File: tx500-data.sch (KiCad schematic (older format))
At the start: 46 parts, among them J1 USB_B_Micro, J2 CAT, J3 REM/DATA, J4 USB_A, U1 TUSB2036, U2 FT232RL, U3 HS-100B, U4 TPS76333, Y1 6MHz

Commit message: Fix floating pins
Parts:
- added R17: 10kΩ, Resistor_SMD:R_1210_3225Metric, symbol Device:R
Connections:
- net labels added: PWREN, SLEEP
- wire segments 155 -> 161
- no-connect marks 59 -> 40
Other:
- note added: "See FT232R datasheet\n6.4 USB Bus Powered with Selectable External Logic Supply"
- note added: "See TUSB2036 datasheet\n9.2.2 Detailed Design Procedure"
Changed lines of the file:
@@
-$EndComp
-$Comp
-L Regulator_Linear:TPS76333 U?
-U 1 1 60701E6D
-P 2250 1200
-AR Path="/6057976E/60701E6D" Ref="U?"  Part="1"
-AR Path="/60701E6D" Ref="U4"  Part="1"
-F 0 "U4" H 2250 1542 50  0000 C CNN
-F 1 "TPS76333" H 2250 1451 50  0000 C CNN
-F 2 "Package_TO_SOT_SMD:SOT-23-5" H 2250 1525 50  0001 C CIN
-F 3 "http://www.ti.com/lit/ds/symlink/tps763.pdf" H 2250 1200 50  0001 C CNN
-F 4 "Voltage Regulator" H 2250 1642 50  0001 C CNN "Description"
-F 5 "TI" H 2250 1642 50  0001 C CNN "Manufacturer_Name"
-F 6 "TPS76333" H 2250 1642 50  0001 C CNN "Manufacturer_Part_Number"
-F 7 "0.97" H 2250 1642 50  0001 C CNN "Price"
-F 8 "595-TPS76333DBVTG4" H 2250 1642 50  0001 C CNN "Vendor Part Number"
-F 9 "Mouser" H 2250 1642 50  0001 C CNN "Vendor"
-	1    2250 1200
-	1    0    0    -1
 $EndComp
 $Comp
@@
 	1400 1150 1400 1100
 Wire Wire Line
-	1400 1100 1950 1100
+	1400 1100 1900 1100
 Wire Wire Line
 	800  1100 1000 1100
@@
 Connection ~ 1400 1100
 Connection ~ 1000 1100
-NoConn ~ 1950 1200
 $Comp
 L Device:R R?
@@
 NoConn ~ 9900 2600
 NoConn ~ 9900 2700
-NoConn ~ 9900 2800
 NoConn ~ 9900 2900
 NoConn ~ 8300 2600
@@
 	9400 6400 9200 6400
 $Comp
-L HS-100B:HS-100B U3
-U 1 1 60A2B59C
-P 8700 6200
-AR Path="/60A2B59C" Ref="U3"  Part="1"
-AR Path="/605AB33C/60A2B59C" Ref="U?"  Part="1"
-F 0 "U3" V 10450 4650 50  0000 R CNN
-F 1 "HS-100B" V 10300 4800 50  0000 R CNN
-F 2 "Package_QFP:LQFP-48_7x7mm_P0.5mm" H 10250 6800 50  0001 L CNN
-F 3 "1.6" H 10250 6700 50  0001 L CNN
-F 4 "USB Audio Interface" H 10250 6600 50  0001 L CNN "Description"
-F 5 "1.6" H 10250 6500 50  0001 L CNN "Height"
-F 6 "Cmedia" H 10250 6400 50  0001 L CNN "Manufacturer_Name"
-F 7 "HS-100B" H 10250 6300 50  0001 L CNN "Manufacturer_Part_Number"
-F 8 "0.78" H 8500 6750 50  0001 C CNN "Price"
-F 9 "HS-100B" H 8500 6750 50  0001 C CNN "Vendor Part Number"
-F 10 "Symmetry" H 8500 6750 50  0001 C CNN "Vendor"
-	1    8700 6200
-	0    -1   -1   0
-$EndComp
-$Comp
 L power:GNDREF #PWR?
 U 1 1 60A2B583
@@
 NoConn ~ 9100 6200
 NoConn ~ 9300 6200
-NoConn ~ 9500 6200
 NoConn ~ 9700 6200
-NoConn ~ 10600 5900
-NoConn ~ 10600 5800
-NoConn ~ 10600 5700
-NoConn ~ 10600 5600
-NoConn ~ 10600 5500
-NoConn ~ 10600 5400
-NoConn ~ 10600 5300
-NoConn ~ 10600 5100
-NoConn ~ 10600 5000
-NoConn ~ 10600 4900
-NoConn ~ 10600 4800
 NoConn ~ 9700 4500
 NoConn ~ 9600 4500
 NoConn ~ 9200 4500
-NoConn ~ 7900 5900
 NoConn ~ 7900 5800
-NoConn ~ 7900 5700
-NoConn ~ 7900 5600
 NoConn ~ 7900 5300
 NoConn ~ 7900 5200
 NoConn ~ 7900 5000
-NoConn ~ 7900 4900
-NoConn ~ 7900 4800
 Wire Wire Line
 	7250 5400 7900 5400
@@
 Text Notes 950  5800 0    118  ~ 0
 PCB
-Text Notes 10300 2750 0    50   ~ 0
+Text Notes 10350 1950 0    50   ~ 0
 See TX-500 adapters\nAudio data cable
 Wire Wire Line
@@
 	-1   0    0    -1
 $EndComp
+$Comp
+L Regulator_Linear:TPS76333 U?
+U 1 1 60701E6D
+P 2250 1200
+AR Path="/6057976E/60701E6D" Ref="U?"  Part="1"
+AR Path="/60701E6D" Ref="U4"  Part="1"
+F 0 "U4" H 2250 1542 50  0000 C CNN
+F 1 "TPS76333" H 2250 1451 50  0000 C CNN
+F 2 "Package_TO_SOT_SMD:SOT-23-5" H 2250 1525 50  0001 C CIN
+F 3 "http://www.ti.com/lit/ds/symlink/tps763.pdf" H 2250 1200 50  0001 C CNN
+F 4 "Voltage Regulator" H 2250 1642 50  0001 C CNN "Description"
+F 5 "TI" H 2250 1642 50  0001 C CNN "Manufacturer_Name"
+F 6 "TPS76333" H 2250 1642 50  0001 C CNN "Manufacturer_Part_Number"
+F 7 "0.97" H 2250 1642 50  0001 C CNN "Price"
+F 8 "595-TPS76333DBVTG4" H 2250 1642 50  0001 C CNN "Vendor Part Number"
+F 9 "Mouser" H 2250 1642 50  0001 C CNN "Vendor"
+	1    2250 1200
+	1    0    0    -1
+$EndComp
+Wire Wire Line
+	1950 1200 1900 1200
+Wire Wire Line
+	1900 1200 1900 1100
+Connection ~ 1900 1100
+Wire Wire Line
+	1900 1100 1950 1100
+$Comp
+L HS-100B:HS-100B U3
+U 1 1 60A2B59C
+P 8700 6200
+AR Path="/60A2B59C" Ref="U3"  Part="1"
+AR Path="/605AB33C/60A2B59C" Ref="U?"  Part="1"
+F 0 "U3" V 10450 4650 50  0000 R CNN
+F 1 "HS-100B" V 10300 4800 50  0000 R CNN
+F 2 "Package_QFP:LQFP-48_7x7mm_P0.5mm" H 10250 6800 50  0001 L CNN
+F 3 "https://datasheet.lcsc.com/szlcsc/1906061502_Cmedia-HS-100B_C371351.pdf" H 10250 6700 50  0001 L CNN
+F 4 "USB Audio Interface" H 10250 6600 50  0001 L CNN "Description"
+F 5 "1.6" H 10250 6500 50  0001 L CNN "Height"
+F 6 "Cmedia" H 10250 6400 50  0001 L CNN "Manufacturer_Name"
+F 7 "HS-100B" H 10250 6300 50  0001 L CNN "Manufacturer_Part_Number"
+F 8 "0.78" H 8500 6750 50  0001 C CNN "Price"
+F 9 "HS-100B" H 8500 6750 50  0001 C CNN "Vendor Part Number"
+F 10 "Symmetry" H 8500 6750 50  0001 C CNN "Vendor"
+	1    8700 6200
+	0    -1   -1   0
+$EndComp
+Text Notes 6400 3350 0    50   ~ 0
+See FT232R datasheet\n6.4 USB Bus Powered with Selectable External Logic Supply
+Text Notes 3800 1200 0    50   ~ 0
+See TUSB2036 datasheet\n9.2.2 Detailed Design Procedure
+Text Label 9900 2800 0    50   ~ 0
+PWREN
+Text Label 9900 2900 0    50   ~ 0
+SLEEP
+$Comp
+L Device:R R?
+U 1 1 605D5F33
+P 10200 2600
+AR Path="/605B3ED2/605D5F33" Ref="R?"  Part="1"
+AR Path="/6059C0E9/605D5F33" Ref="R?"  Part="1"
+AR Path="/605D5F33" Ref="R17"  Part="1"
+F 0 "R17" H 10270 2646 50  0000 L CNN
+F 1 "10kΩ" H 10270 2555 50  0000 L CNN
+F 2 "Resistor_SMD:R_1210_3225Metric" V 10130 2600 50  0001 C CNN
+F 3 "https://www.mouser.com/datasheet/2/427/rcae3-1761931.pdf" H 10200 2600 50  0001 C CNN
+F 4 "Vishay" H 10270 2746 50  0001 C CNN "Manufacturer_Name"
+F 5 "RCA121015K0FKEA" H 10270 2746 50  0001 C CNN "Manufacturer_Part_Number"
+F 6 "0.11" H 10270 2746 50  0001 C CNN "Price"
+F 7 "71-RCA121015K0FKEA" H 10270 2746 50  0001 C CNN "Vendor Part Number"
+F 8 "Mouser" H 10270 2746 50  0001 C CNN "Vendor"
+	1    10200 2600
+	1    0    0    -1
+$EndComp
+Wire Wire Line
+	10200 2750 10200 2800
+Wire Wire Line
+	10200 2800 9900 2800
+Wire Wire Line
+	10200 2450 10650 2450
 $EndSCHEMATC

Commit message: Add case ground
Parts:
- added C18: 4.7μF, Capacitor_SMD:C_1210_3225Metric, symbol Device:C
- added C19: 120μF, Capacitor_SMD:C_1210_3225Metric, symbol Device:C
- C11, C16, C17: value 100μF -> 120μF; Manufacturer_Name AVX -> (none); Manufacturer_Part_Number TACT107M006XTA -> (none); Price 4.4 -> (none); Vendor Mouser -> (none); Vendor Part Number 581-TACT107M006XTA -> (none)
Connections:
- net labels added: GND1
- wire segments 161 -> 171
- no-connect marks 40 -> 38
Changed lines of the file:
@@
 L power:GNDREF #PWR?
 U 1 1 6055B654
-P 1200 3350
+P 1200 3150
 AR Path="/6057976E/6055B654" Ref="#PWR?"  Part="1"
 AR Path="/6055B654" Ref="#PWR0116"  Part="1"
-F 0 "#PWR0116" H 1200 3100 50  0001 C CNN
-F 1 "GNDREF" H 1205 3177 50  0001 C CNN
-F 2 "" H 1200 3350 50  0001 C CNN
-F 3 "" H 1200 3350 50  0001 C CNN
-	1    1200 3350
+F 0 "#PWR0116" H 1200 2900 50  0001 C CNN
+F 1 "GNDREF" H 1205 2977 50  0001 C CNN
+F 2 "" H 1200 3150 50  0001 C CNN
+F 3 "" H 1200 3150 50  0001 C CNN
+	1    1200 3150
 	1    0    0    -1
 $EndComp
@@
 	2600 2750 2600 2600
 Wire Wire Line
-	1200 3000 1200 3350
+	1200 3000 1200 3150
 Wire Wire Line
 	1950 2700 2200 2700
@@
 Connection ~ 2600 2600
 Connection ~ 2200 2700
-NoConn ~ 1100 3000
 $Comp
 L Connector:USB_B_Micro J?
@@
 	-1   0    0    -1
 $EndComp
-NoConn ~ 4800 7200
 Connection ~ 4050 6250
 Wire Wire Line
@@
 AR Path="/605FD4EC" Ref="C16"  Part="1"
 F 0 "C16" H 9615 1046 50  0000 L CNN
-F 1 "100μF" H 9615 955 50  0000 L CNN
+F 1 "120μF" H 9615 955 50  0000 L CNN
 F 2 "Capacitor_SMD:C_1210_3225Metric" H 9538 850 50  0001 C CNN
-F 3 "https://www.mouser.com/datasheet/2/40/tac-776418.pdf" H 9500 1000 50  0001 C CNN
-F 4 "AVX" H 9615 1146 50  0001 C CNN "Manufacturer_Name"
-F 5 "TACT107M006XTA" H 9615 1146 50  0001 C CNN "Manufacturer_Part_Number"
-F 6 "4.4" H 9615 1146 50  0001 C CNN "Price"
-F 7 "581-TACT107M006XTA" H 9615 1146 50  0001 C CNN "Vendor Part Number"
-F 8 "Mouser" H 9615 1146 50  0001 C CNN "Vendor"
+F 3 "" H 9500 1000 50  0001 C CNN
+F 4 "" H 9615 1146 50  0001 C CNN "Manufacturer_Name"
+F 5 "" H 9615 1146 50  0001 C CNN "Manufacturer_Part_Number"
+F 6 "" H 9615 1146 50  0001 C CNN "Price"
+F 7 "" H 9615 1146 50  0001 C CNN "Vendor Part Number"
+F 8 "" H 9615 1146 50  0001 C CNN "Vendor"
 	1    9500 1000
 	1    0    0    -1
@@
 AR Path="/60A2B566" Ref="C11"  Part="1"
 F 0 "C11" H 8115 4246 50  0000 L CNN
-F 1 "100μF" H 8115 4155 50  0000 L CNN
+F 1 "120μF" H 8115 4155 50  0000 L CNN
 F 2 "Capacitor_SMD:C_1210_3225Metric" H 8038 4050 50  0001 C CNN
-F 3 "https://www.mouser.com/datasheet/2/40/tac-776418.pdf" H 8000 4200 50  0001 C CNN
-F 4 "AVX" H 8115 4346 50  0001 C CNN "Manufacturer_Name"
-F 5 "TACT107M006XTA" H 8115 4346 50  0001 C CNN "Manufacturer_Part_Number"
-F 6 "4.4" H 8115 4346 50  0001 C CNN "Price"
-F 7 "581-TACT107M006XTA" H 8115 4346 50  0001 C CNN "Vendor Part Number"
-F 8 "Mouser" H 8115 4346 50  0001 C CNN "Vendor"
+F 3 "" H 8000 4200 50  0001 C CNN
+F 4 "" H 8115 4346 50  0001 C CNN "Manufacturer_Name"
+F 5 "" H 8115 4346 50  0001 C CNN "Manufacturer_Part_Number"
+F 6 "" H 8115 4346 50  0001 C CNN "Price"
+F 7 "" H 8115 4346 50  0001 C CNN "Vendor Part Number"
+F 8 "" H 8115 4346 50  0001 C CNN "Vendor"
 	1    8000 4200
 	1    0    0    -1
@@
 AR Path="/605B3ED2/605A97F2" Ref="C?"  Part="1"
 F 0 "C17" H 4165 6446 50  0000 L CNN
-F 1 "100μF" H 4165 6355 50  0000 L CNN
+F 1 "120μF" H 4165 6355 50  0000 L CNN
 F 2 "Capacitor_SMD:C_1210_3225Metric" H 4088 6250 50  0001 C CNN
-F 3 "https://www.mouser.com/datasheet/2/40/tac-776418.pdf" H 4050 6400 50  0001 C CNN
-F 4 "AVX" H 3935 6546 50  0001 C CNN "Manufacturer_Name"
-F 5 "TACT107M006XTA" H 3935 6546 50  0001 C CNN "Manufacturer_Part_Number"
-F 6 "4.4" H 3935 6546 50  0001 C CNN "Price"
-F 7 "581-TACT107M006XTA" H 3935 6546 50  0001 C CNN "Vendor Part Number"
-F 8 "Mouser" H 3935 6546 50  0001 C CNN "Vendor"
+F 3 "" H 4050 6400 50  0001 C CNN
+F 4 "" H 3935 6546 50  0001 C CNN "Manufacturer_Name"
+F 5 "" H 3935 6546 50  0001 C CNN "Manufacturer_Part_Number"
+F 6 "" H 3935 6546 50  0001 C CNN "Price"
+F 7 "" H 3935 6546 50  0001 C CNN "Vendor Part Number"
+F 8 "" H 3935 6546 50  0001 C CNN "Vendor"
 	1    4050 6400
 	-1   0    0    -1
@@
 Wire Wire Line
 	10200 2450 10650 2450
+$Comp
+L Device:C C?
+U 1 1 606059E5
+P 2800 1300
+AR Path="/6057976E/606059E5" Ref="C?"  Part="1"
+AR Path="/606059E5" Ref="C18"  Part="1"
+F 0 "C18" H 2685 1346 50  0000 R CNN
+F 1 "4.7μF" H 2685 1255 50  0000 R CNN
+F 2 "Capacitor_SMD:C_1210_3225Metric" H 2838 1150 50  0001 C CNN
+F 3 "https://www.mouser.com/datasheet/2/210/WTC_MLCC_General_Purpose-1534899.pdf" H 2800 1300 50  0001 C CNN
+F 4 "Walsin" H 2915 1446 50  0001 C CNN "Manufacturer_Name"
+F 5 "1210F475Z500CT" H 2915 1446 50  0001 C CNN "Manufacturer_Part_Number"
+F 6 "0.62" H 2915 1446 50  0001 C CNN "Price"
+F 7 "791-1210F475Z500CT" H 2915 1446 50  0001 C CNN "Vendor Part Number"
+F 8 "Mouser" H 2915 1446 50  0001 C CNN "Vendor"
+	1    2800 1300
+	1    0    0    -1
+$EndComp
+Connection ~ 2800 1100
+Wire Wire Line
+	2250 1500 2800 1500
+Wire Wire Line
+	2800 1500 2800 1450
+Connection ~ 2250 1500
+Wire Wire Line
+	2800 1100 2800 1150
+$Comp
+L Device:C C?
+U 1 1 6065220F
+P 1700 2100
+AR Path="/6059C0E9/6065220F" Ref="C?"  Part="1"
+AR Path="/6065220F" Ref="C19"  Part="1"
+F 0 "C19" H 1815 2146 50  0000 L CNN
+F 1 "120μF" H 1815 2055 50  0000 L CNN
+F 2 "Capacitor_SMD:C_1210_3225Metric" H 1738 1950 50  0001 C CNN
+F 3 "" H 1700 2100 50  0001 C CNN
+F 4 "" H 1815 2246 50  0001 C CNN "Manufacturer_Name"
+F 5 "" H 1815 2246 50  0001 C CNN "Manufacturer_Part_Number"
+F 6 "" H 1815 2246 50  0001 C CNN "Price"
+F 7 "" H 1815 2246 50  0001 C CNN "Vendor Part Number"
+F 8 "" H 1815 2246 50  0001 C CNN "Vendor"
+	1    1700 2100
+	1    0    0    -1
+$EndComp
+Wire Wire Line
+	1500 1950 1700 1950
+Connection ~ 1500 1950
+$Comp
+L power:GNDREF #PWR?
+U 1 1 6065EA82
+P 1700 2250
+AR Path="/6057976E/6065EA82" Ref="#PWR?"  Part="1"
+AR Path="/6065EA82" Ref="#PWR0129"  Part="1"
+F 0 "#PWR0129" H 1700 2000 50  0001 C CNN
+F 1 "GNDREF" H 1705 2077 50  0001 C CNN
+F 2 "" H 1700 2250 50  0001 C CNN
+F 3 "" H 1700 2250 50  0001 C CNN
+	1    1700 2250
+	1    0    0    -1
+$EndComp
+$Comp
+L power:GND1 #PWR?
+U 1 1 60676C56
+P 900 3150
+F 0 "#PWR?" H 900 2900 50  0001 C CNN
+F 1 "GND1" H 905 2977 50  0001 C CNN
+F 2 "" H 900 3150 50  0001 C CNN
+F 3 "" H 900 3150 50  0001 C CNN
+	1    900  3150
+	1    0    0    -1
+$EndComp
+Wire Wire Line
+	900  3150 900  3100
+Wire Wire Line
+	900  3100 1100 3100
+Wire Wire Line
+	1100 3100 1100 3000
+$Comp
+L power:GND1 #PWR?
+U 1 1 6068B8FC
+P 5000 7350
+F 0 "#PWR?" H 5000 7100 50  0001 C CNN
+F 1 "GND1" H 5005 7177 50  0001 C CNN
+F 2 "" H 5000 7350 50  0001 C CNN
+F 3 "" H 5000 7350 50  0001 C CNN
+	1    5000 7350
+	1    0    0    -1
+$EndComp
+Wire Wire Line
+	4800 7200 4800 7300
+Wire Wire Line
+	4800 7300 5000 7300
+Wire Wire Line
+	5000 7300 5000 7350
 $EndSCHEMATC

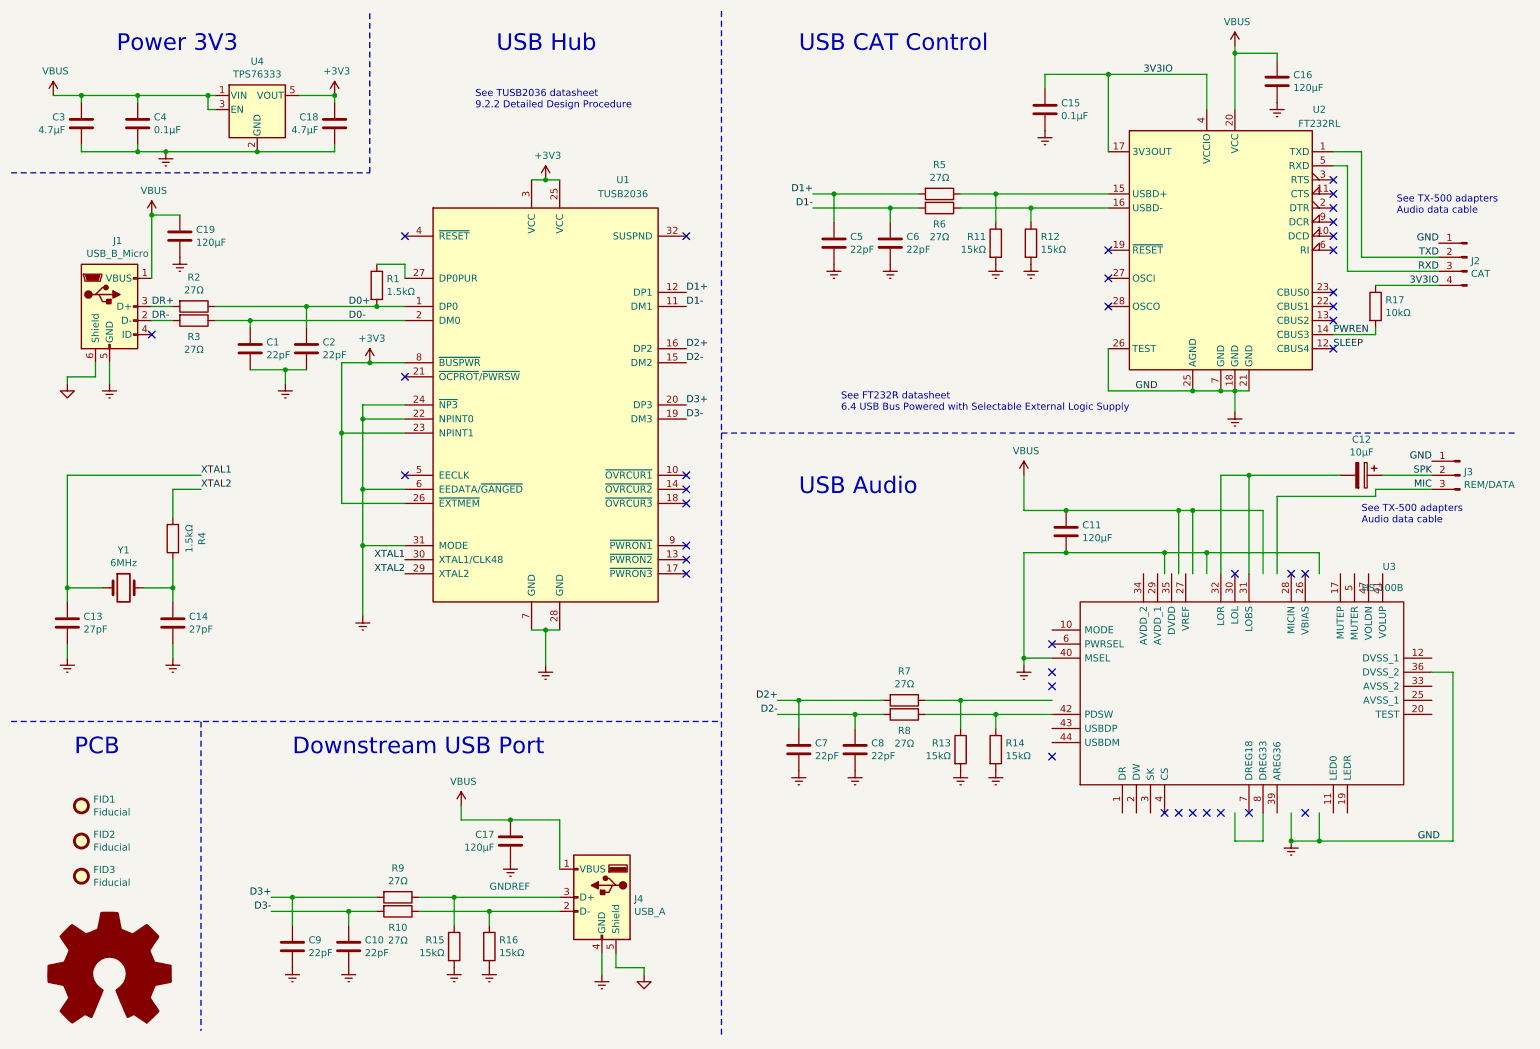
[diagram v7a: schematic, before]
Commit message: Clean up HS-100B pins
Add test points
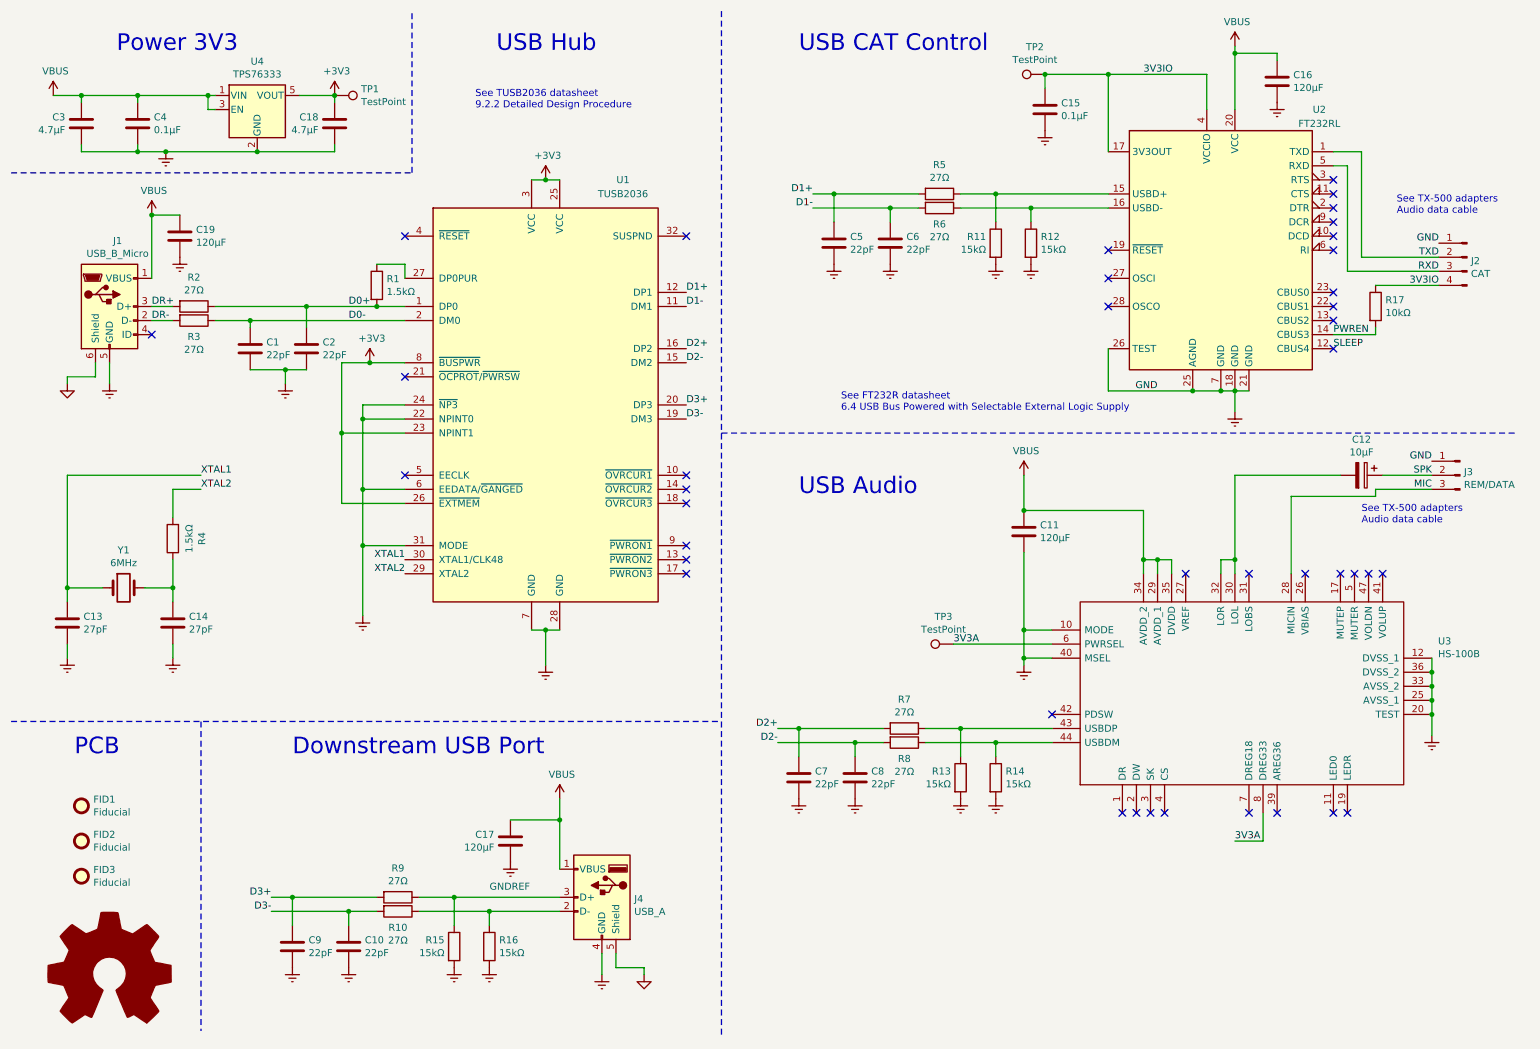
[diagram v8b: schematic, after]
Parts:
- added TP1, TP2, TP3: TestPoint, TestPoint:TestPoint_Pad_D1.0mm, symbol Connector:TestPoint
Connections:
- net labels added: 3V3A
- wire segments 171 -> 165
- no-connect marks 38 -> 40
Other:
- moved on the sheet: C11, C7, C8, R13, R14, R7, R8
